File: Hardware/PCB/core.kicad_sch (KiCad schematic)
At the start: 26 parts, among them IC3 ATxmega32A4U-A, IC4 741G126DBVAHC, J2 OUT0, Q1 BC817-40W, Q2 NTF2955T1G, U1 ID-12/20SMD

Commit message: versão 1.3 final & ficheiros de manufacturing
- ainda sem revisão do Filipe
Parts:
- removed IC4: 741G126DBVAHC, Package_TO_SOT_SMD:SOT-23-5, symbol harp rfid reader:741G126DBV
- added C22, C30: 100nF, Capacitor_SMD:C_0402_1005Metric, symbol Device:C
- added IC10, IC4, IC5: SN74LVC1G125DBVT, Package_TO_SOT_SMD:SOT-23-5, symbol 74xGxx:SN74LVC1G125DBV
- added J3: NPPN051BFLD-RC, Connector_PinSocket_2.00mm:PinSocket_1x05_P2.00mm_Vertical_SMD_Pin1Right, symbol Connector:Conn_01x05_Socket
- added J4: NPPN071BFLC-RC, Connector_PinSocket_2.00mm:PinSocket_1x07_P2.00mm_Vertical_SMD_Pin1Right, symbol Connector:Conn_01x07_Socket
- added R11, R16: 10k, Resistor_SMD:R_0402_1005Metric, symbol Device:R_US
- added R14, R15: 0R, Resistor_SMD:R_0402_1005Metric, symbol Device:R_US
- C12, C13, C14, C15, C16, C21: OEPSPN (none) -> OEPS010016; TempCo (none) -> X7R; Tolerance (none) -> ±10%; Voltage (none) -> 50V
- D1: value TAG_B0 -> 5975004407F; OEPSPN (none) -> OEPS030006
- D2: value TAG_T0 -> 5975004407F; OEPSPN (none) -> OEPS030006
- D3: value STATE -> 5975004407F; OEPSPN (none) -> OEPS030006
- D4: value OUTLED -> 5975004407F; OEPSPN (none) -> OEPS030006
- IC3: MPN DNI ????? -> ATXMEGA32A4U-A; OEPSPN (none) -> OEPS080012
- J2: value OUT0 -> 282834-2
- PDI0: value MA03-2 -> 67996-206HLF; MPN (none) -> 67996-206HLF; OEPSPN (none) -> OEPS070015
- Q1: MPN BC817-40W-7 -> BC817-40W-7; OEPSPN (none) -> OEPS060005; Voltage (none) -> 45V
- Q2: Voltage (none) -> 60V
- R2, R3, R4, R6, R8: OEPSPN (none) -> OEPS020027; Tolerance (none) -> ±1%
- R5: OEPSPN (none) -> OEPS020030; Tolerance (none) -> ±1%
- R7: value 75 >1/4W -> 39R; OEPSPN (none) -> OEPS020034; Tolerance (none) -> ±1%
- SP1: value BUZZER-COIL_SMT-0540-S-R -> SMT-0540-S-R; OEPSPN (none) -> OEPS100012
- U1: footprint harp rfid reader:ID-12_SMD -> harp rfid reader:ID-12_SMD body; MPN (none) -> ID-12LA; OEPSPN (none) -> OEPS100013; now not fitted; now left out of the parts list
- X1: renamed from OSC1; value CNP-MISCELLANEOUS_OSCILLATOR -> O 32,0-JT32C-A-K-3,3-LF; MPN O 32,0-JT32C-A-K-3,3-LF -> O 32,0-JT32C-A-K-3,3-LF; OEPSPN (none) -> OEPS080014
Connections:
- net VDDIO is gone; now on net +3V3: C12.1, C13.1, C14.1, C15.1, C16.1, IC3.19 (VCC), IC3.31 (VCC), IC3.39 (AVCC), IC3.9 (VCC), PDI0.2 (Pin_2), U1.2 (RES), X1.4 (Vdd)
- net +3V3: now also C22.1, C30.1, IC10.5 (VCC), IC5.5 (VCC), J3.2 (Pin_2); no longer U1.11 (5V)
- net +5V: now also IC4.5 (VCC)
- net F2: now also IC5.2, J4.7 (Pin_7), R11.1, R15.2; no longer IC3.13 (PC3)
- net GND: now also C22.2, C30.2, IC10.1, IC10.3 (GND), IC4.1, IC4.3 (GND), IC5.1, IC5.3 (GND), J3.1 (Pin_1), J4.6 (Pin_6), R11.2, R16.2
- net OUT0: now also IC4.2
- net TX: now also IC10.2, J4.4 (Pin_4), R14.2, R16.1; no longer IC3.22 (PD2)
- net at J2.1 (Pin_1): now also IC4.4
- net at U1.10 (LED): now also J4.3 (Pin_3)
- net at U1.3 (ANT1): now also J3.3 (Pin_3)
- net at U1.4 (ANT2): now also J3.4 (Pin_4)
- net at U1.5 (CP): now also J3.5 (Pin_5)
- net at U1.8 (D1): now also J4.5 (Pin_5)
- new net UC_F2: IC3.13 (PC3), IC5.4, R15.1
- new net UC_TX: IC10.4, IC3.22 (PD2), R14.1
- new net VRFID: J4.1 (Pin_1), U1.11 (5V)
- no-connect marks 1 -> 2
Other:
- moved on the sheet: C12, C13, C14, C15, C16, C21, D1, D2, D3, D4, IC3, J2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

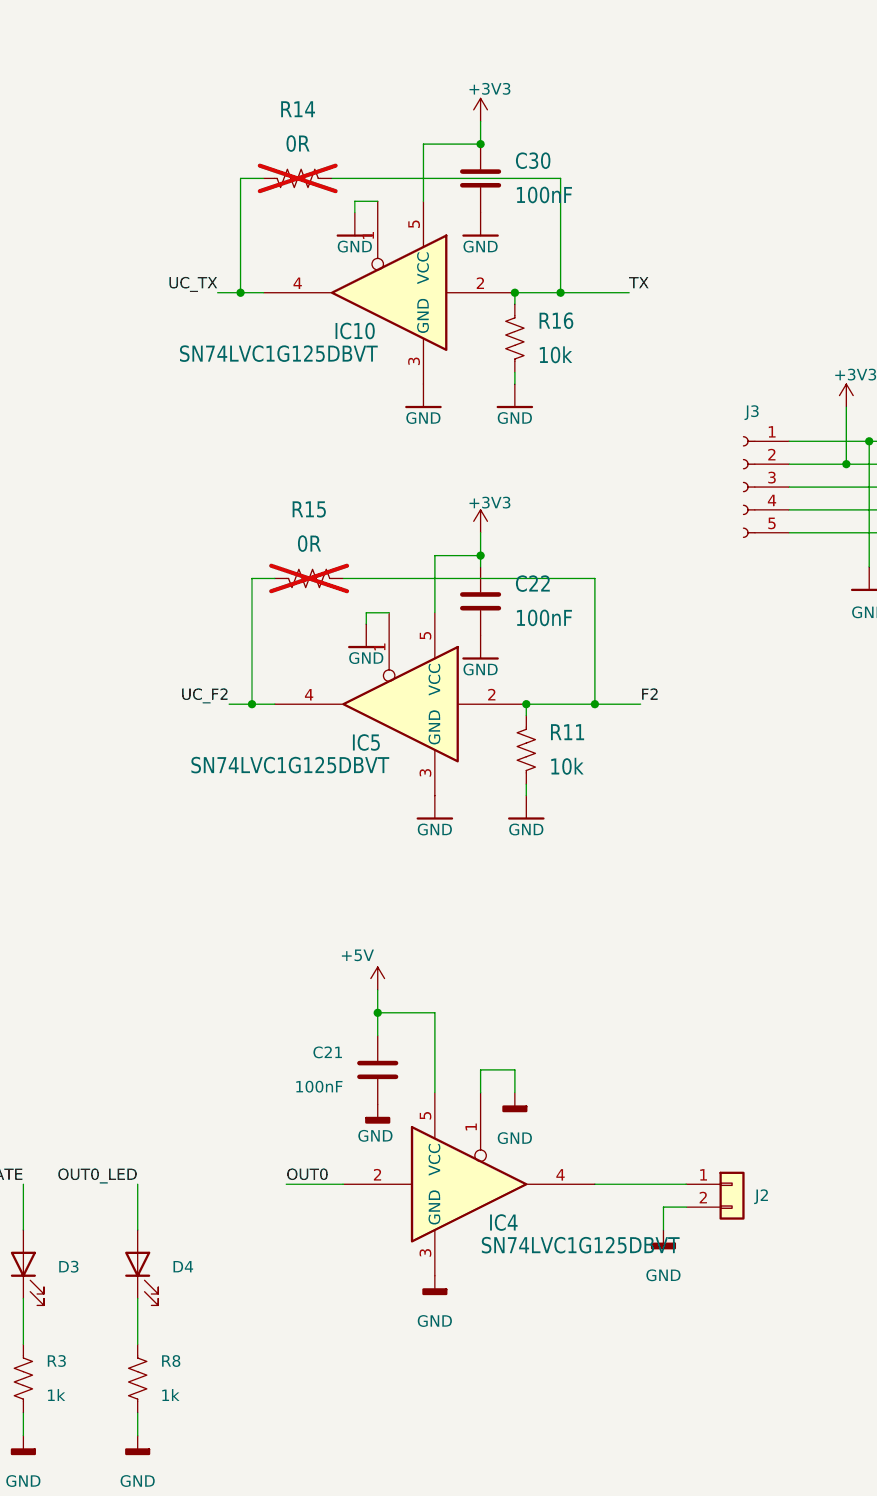
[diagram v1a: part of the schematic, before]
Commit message: para revisão Filipe
ficheiros de manufacturing criados
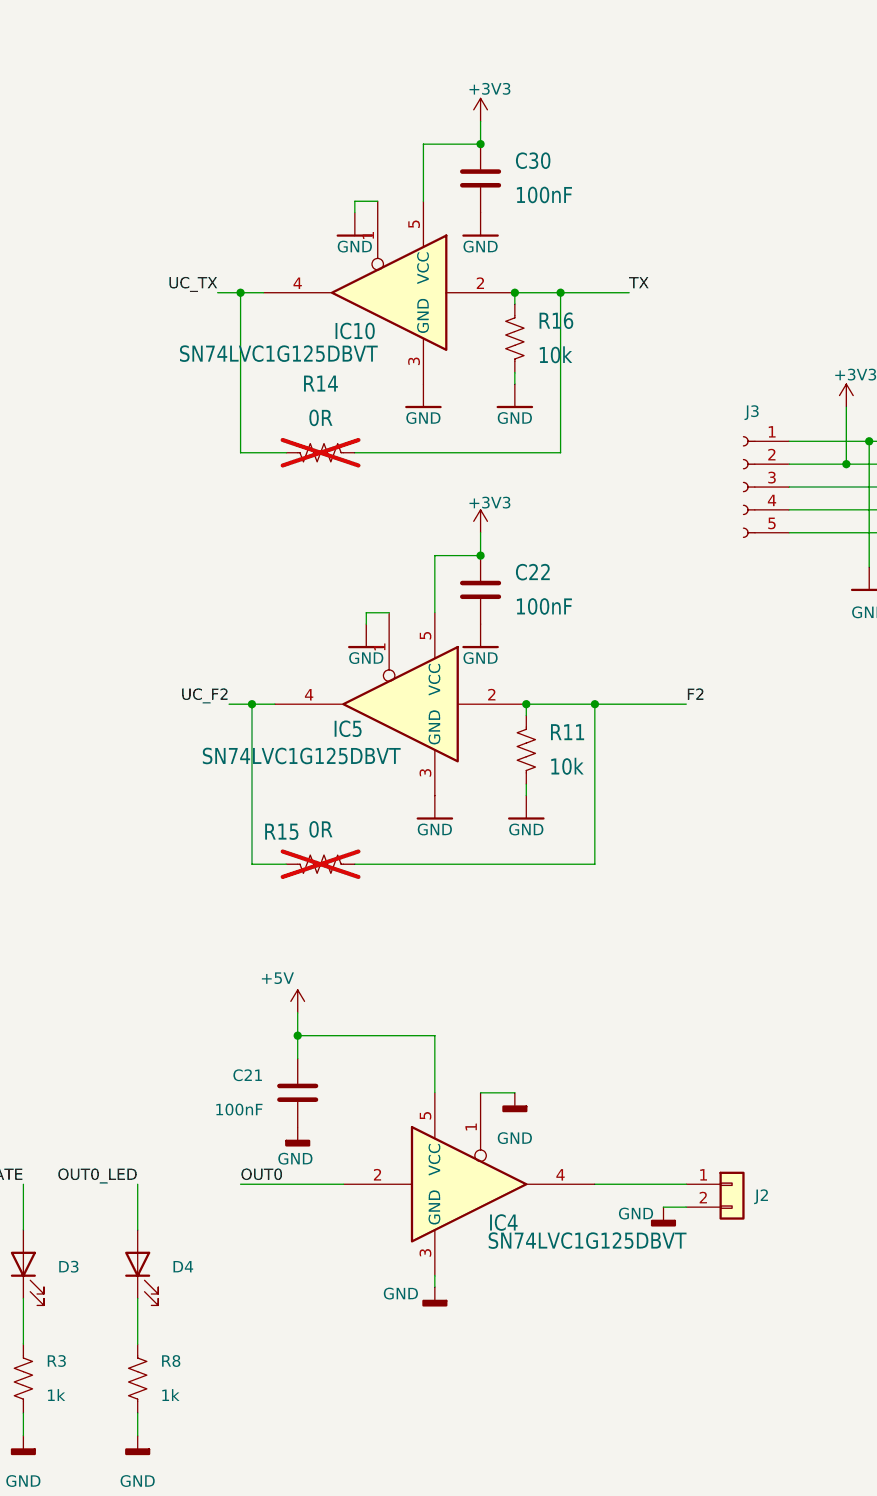
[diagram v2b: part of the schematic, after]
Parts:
- C12, C13, C14, C15, C16, C21, C22, C30: OEPS Description (none) -> CAPACITOR: SMD CER 0402 100nF 50V ±10% X7R [CGA2B3X7R1H104K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; OEPS PN (none) -> OEPS010016; OEPSPN OEPS010016 -> (none)
- D1, D2, D3, D4: OEPS Description (none) -> DIODE: LED 0603 Red 635nm 20mA [5975004407F] [0603]; OEPS PN (none) -> OEPS030006; OEPSPN OEPS030006 -> (none)
- IC10, IC4, IC5: OEPS Description (none) -> IC: BUFFER NON-INVERT 1CH 3-STATE [SN74LVC1G125DBVT] [SOT-2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; OEPS PN (none) -> OEPS080029; OEPSPN OEPS080029 -> (none)
- IC3: OEPS Description (none) -> IC: MCU ATXMEGA A4U 8bits 32KB [ATXMEGA32A4U-A] [TQFP-44]; OEPS PN (none) -> OEPS080012; OEPSPN OEPS080012 -> (none)
- J2: OEPS Description (none) -> CONNECTOR: TERMINAL BLOCK 2.54MM 2POS side entry [282834-2]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; OEPS PN (none) -> OEPS070020; OEPSPN OEPS070020 -> (none)
- J3: OEPS Description (none) -> CONNECTOR: HEADER 2.00MM straight 1x5POS GOLD [NPPN051BFLD-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; OEPS PN (none) -> OEPS070018; OEPSPN OEPS070018 -> (none)
- J4: MPN ‎NPPN071BFLC-RC‎ -> NPPN071BFLC-RC; OEPS Description (none) -> CONNECTOR: HEADER 2.00MM straight 1x7POS GOLD [NPPN071BFLC-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; OEPS PN (none) -> OEPS070019; OEPSPN OEPS070019 -> (none)
- PDI0: OEPS Description (none) -> CONNECTOR: HEADER 2.54MM straight 2x3POS [67996-206HLF] [TH]; OEPS PN (none) -> OEPS070015; OEPSPN OEPS070015 -> (none)
- Q1: OEPS Description (none) -> TRANSISTOR: BJT NPN 45V 0.5A [BC817-40W-7] [SOT-323]; OEPS PN (none) -> OEPS060005; OEPSPN OEPS060005 -> (none)
- Q2: OEPS Description (none) -> TRANSISTOR: MOSFET P-CH 60V 1.7A [NTF2955T1G] [SOT-223]; OEPS PN (none) -> OEPS060004; OEPSPN OEPS060004 -> (none)
- R11, R16, R5: OEPS Description (none) -> RESISTOR: SMD 0402 10kΩ ±1% 0.063W [CRCW040210K0FKED] [SMD]; OEPS PN (none) -> OEPS020030; OEPSPN OEPS020030 -> (none)
- R14, R15: MPN RC0402JR-070RL -> DNP; OEPS Description (none) -> DNP: Do Not Populate (DNI); OEPS PN (none) -> OEPS000000; OEPSPN OEPS020001 -> (none); Tolerance (none) -> ±0.1%
- R2, R3, R4, R6, R8: OEPS Description (none) -> RESISTOR: SMD 0402 1kΩ ±1% 0.063W [CRCW04021K00FKED] [SMD]; OEPS PN (none) -> OEPS020027; OEPSPN OEPS020027 -> (none)
- R7: OEPS Description (none) -> RESISTOR: SMD 0402 39Ω ±1% 0.250W [RCS040239R0FKED] [SMD]; OEPS PN (none) -> OEPS020034; OEPSPN OEPS020034 -> (none)
- SP1: OEPS Description (none) -> OTHER: BUZZER MAGNETIC 3V 5X5MM SMD [SMT-0540-S-R] [SMD]; OEPS PN (none) -> OEPS100012; OEPSPN OEPS100012 -> (none)
- U1: OEPS Description (none) -> OTHER: RFID Reader ID-12LA (125 kHz) [ID-12LA] [TH]; OEPS PN (none) -> OEPS100013; OEPSPN OEPS100013 -> (none)
- X1: OEPS Description (none) -> IC: XTAL OSC TCXO 32MHz HCMOS 2.5ppm [O 32,0-JT32C-A-K-3,3-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; OEPS PN (none) -> OEPS080014; OEPSPN OEPS080014 -> (none)
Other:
- moved on the sheet: C21, C22, R14, R15
